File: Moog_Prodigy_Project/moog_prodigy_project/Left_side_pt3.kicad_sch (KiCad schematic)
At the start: 58 parts, among them SW7 SW_Slide_DPDT, U12B MCP6562, U13 NE5532, U14 AD8001AR, U14C BF244A, U14E? 4007, U2 NE5532, U2B2 OPA134

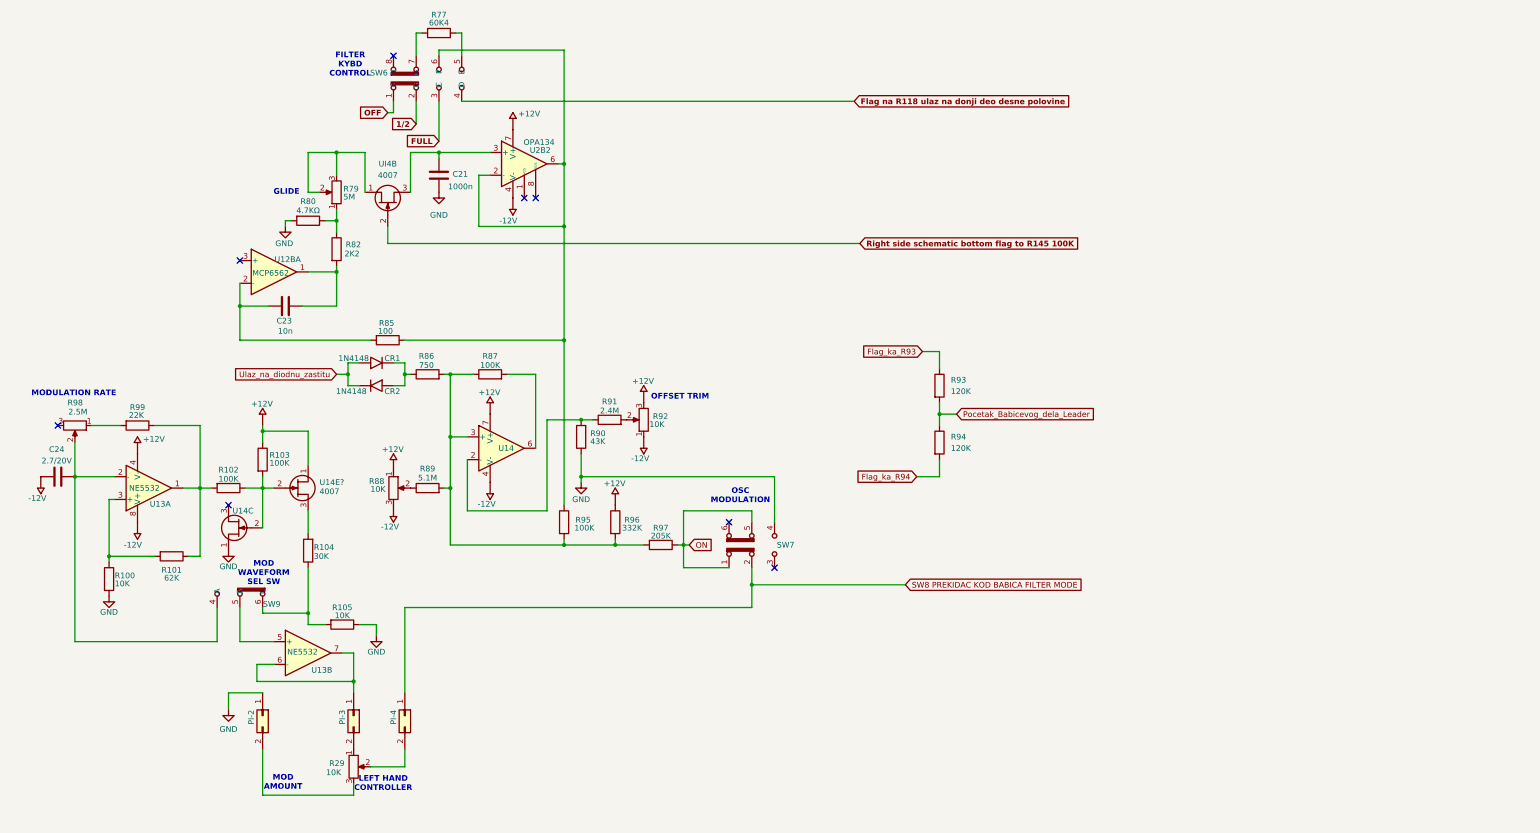
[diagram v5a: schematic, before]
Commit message: KiCad smybols import CA3046
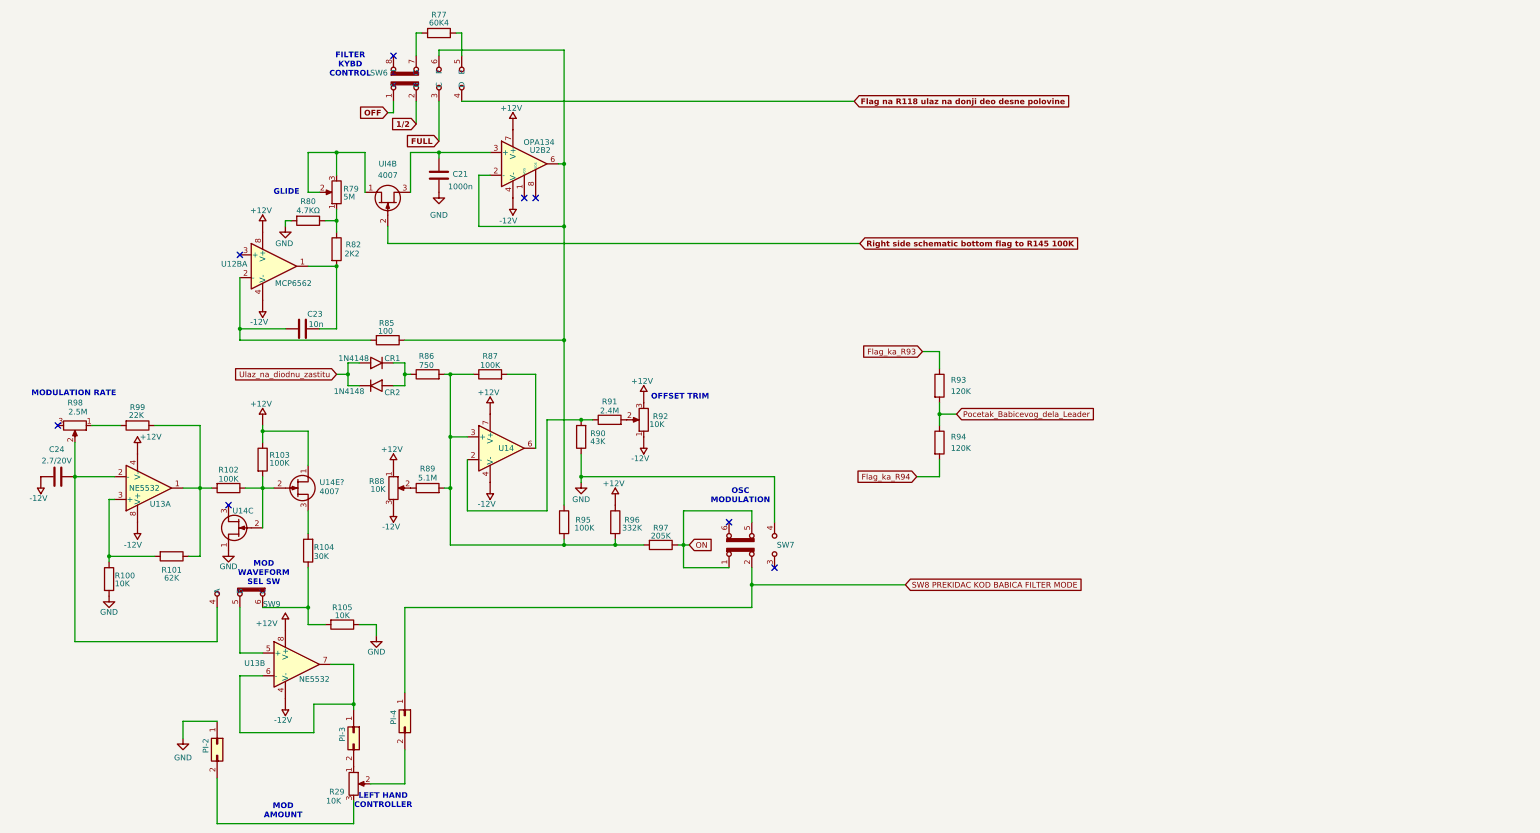
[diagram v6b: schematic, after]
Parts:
- removed Vcc__minus_17, Vcc__minus_20: -12V, symbol power:napajanje
- removed Vcc__plus_13, Vcc__plus_17, Vcc__plus_24, Vcc__plus_25, Vcc__plus_26, Vcc__plus_27, Vcc__plus_28: +12V, symbol power:napajanje
- added unit 3 of U13
- added U34, U35, U36, U37, U38, U39, U40, U68, U72: +12V, symbol Power_supply:Vcc_reference
- added U67: MCP6562, symbol Comparator:MCP6562
- added U69, U70, U71: -12V, symbol Power_supply:Vcc_reference
- added Vcc__minus_1: -12V, symbol power:napajanje
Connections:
- net at R103.1, U14E?.1 (D): now also U38.
- net at U2B2.7 (V+): now also U34.
- net at R96.1: now also U36.
- net at U14.7 (V+): now also U40.
- net at R88.1: now also U37.
- net at C24.2: now also U70.
- net at R88.3: now also U71.
- net at U2.4 (V-): now also U39.
- net at R92.3: now also U35.
- new net: U67.4 (V-), Vcc__minus_1.
- new net: U67.8 (V+), U68.
- new net: U13.8 (V+), U72.
- new net: U13.4 (V-), U69.
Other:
- moved on the sheet: C23, PI-2, PI-3, R29, U12BA, U13B

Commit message: Vcc fix, banana jack, connector, OP adding top sch
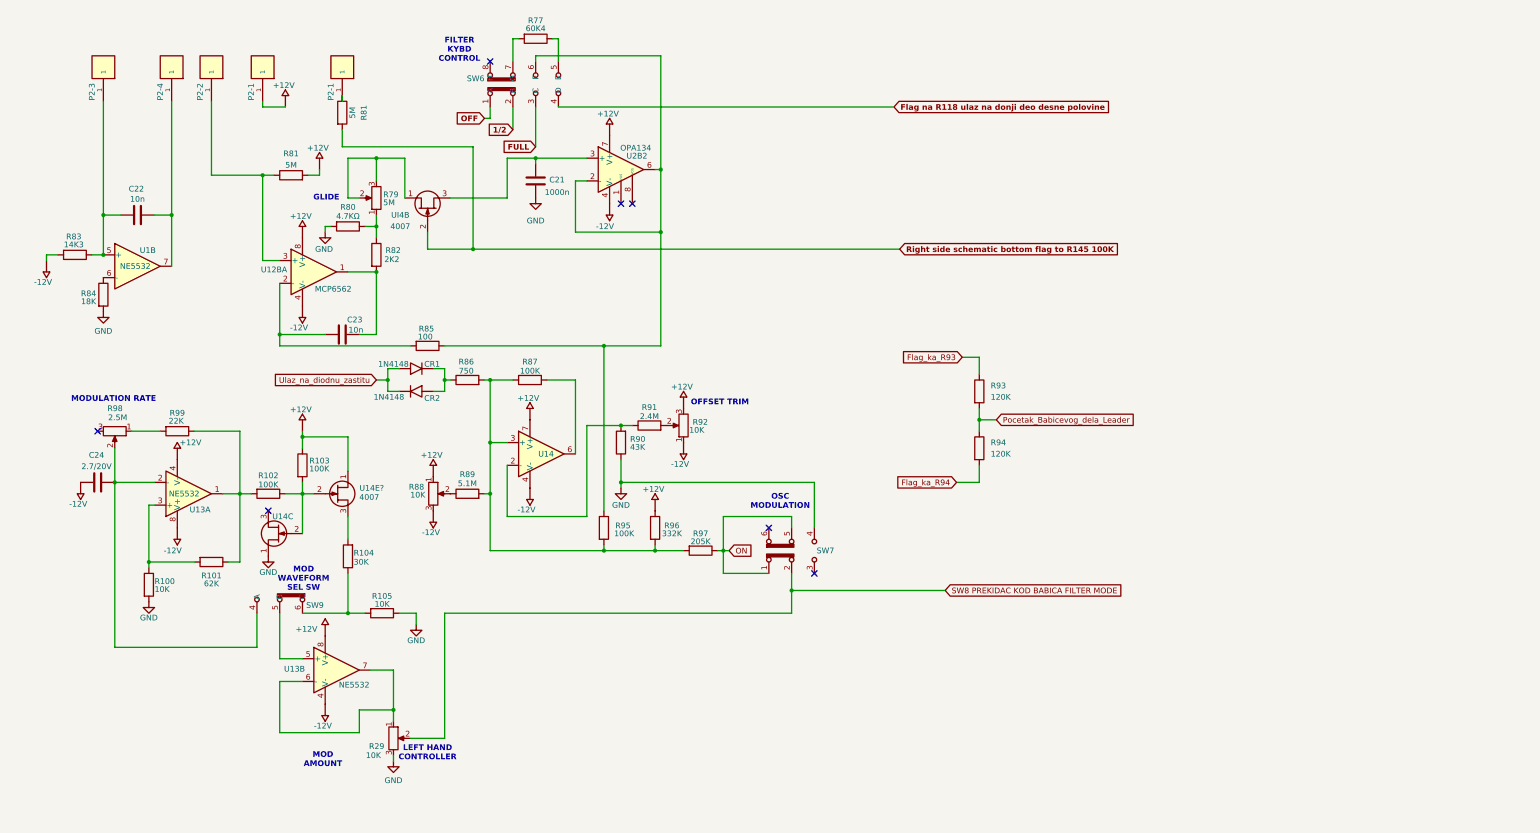
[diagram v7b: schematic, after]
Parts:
- removed PI-2, PI-3, PI-4: Conn_02x01, symbol Connector_Generic:Conn_02x01
- added C22: 10n, symbol Device:C
- added J1: P2-3, CT3151-2:CALTEST_CT3151-2, symbol CT3151-2:CT3151-2
- added J2: P2-4, CT3151-2:CALTEST_CT3151-2, symbol CT3151-2:CT3151-2
- added J3: P2-2, CT3151-2:CALTEST_CT3151-2, symbol CT3151-2:CT3151-2
- added J4, J5: P2-1, CT3151-2:CALTEST_CT3151-2, symbol CT3151-2:CT3151-2
- added R81 (x2): 5M, symbol Device:R
- added R83: 14K3, symbol Device:R
- added R84: 18K, symbol Device:R
- added U1: NE5532, symbol Amplifier_Operational:NE5532
- added U73, U74: +12V, symbol Power_supply:Vcc_reference
- added Vcc__minus_2: -12V, symbol power:napajanje
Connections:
- net GND: now also R29.3, R84.2
- net Right side schematic bottom flag to R145 100K: now also R81.2
- net SW8 PREKIDAC KOD BABICA FILTER MODE: now also R29.2
- net at U13.6 (-), U13.7: now also R29.1
- net at U12B.3 (+): now also J3.1, J3.2 (1), J3.3 (1), J3.4 (1), R81.1
- new net: J5.1, J5.2 (1), J5.3 (1), J5.4 (1), U74.
- new net: R84.1, U1.6 (-)
- new net: C22.2, J1.1, J1.2 (1), J1.3 (1), J1.4 (1), R83.1, U1.5 (+)
- new net: R83.2, Vcc__minus_2.
- new net: J4.1, J4.2 (1), J4.3 (1), J4.4 (1), R81.1
- new net: R81.2, U73.
- new net: C22.1, J2.1, J2.2 (1), J2.3 (1), J2.4 (1), U1.7
- no-connect marks 8 -> 7
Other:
- moved on the sheet: C21, C23, C24, CR1, CR2, R100, R101, R102, R103, R104, R105, R29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

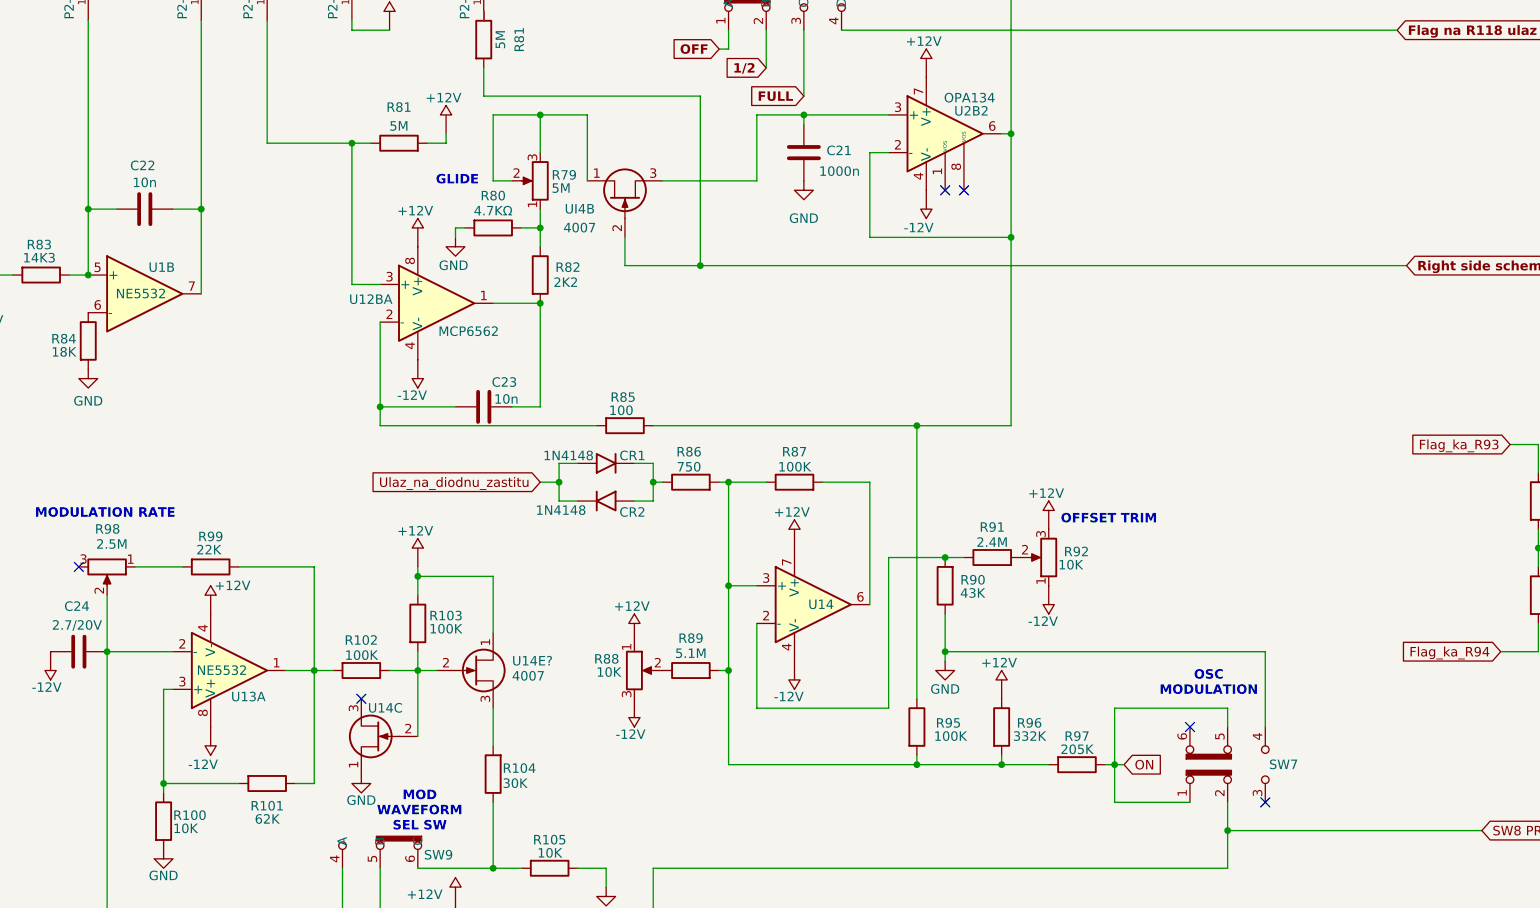
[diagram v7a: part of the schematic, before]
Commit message: 4007 update, impor biblioteka LM 393
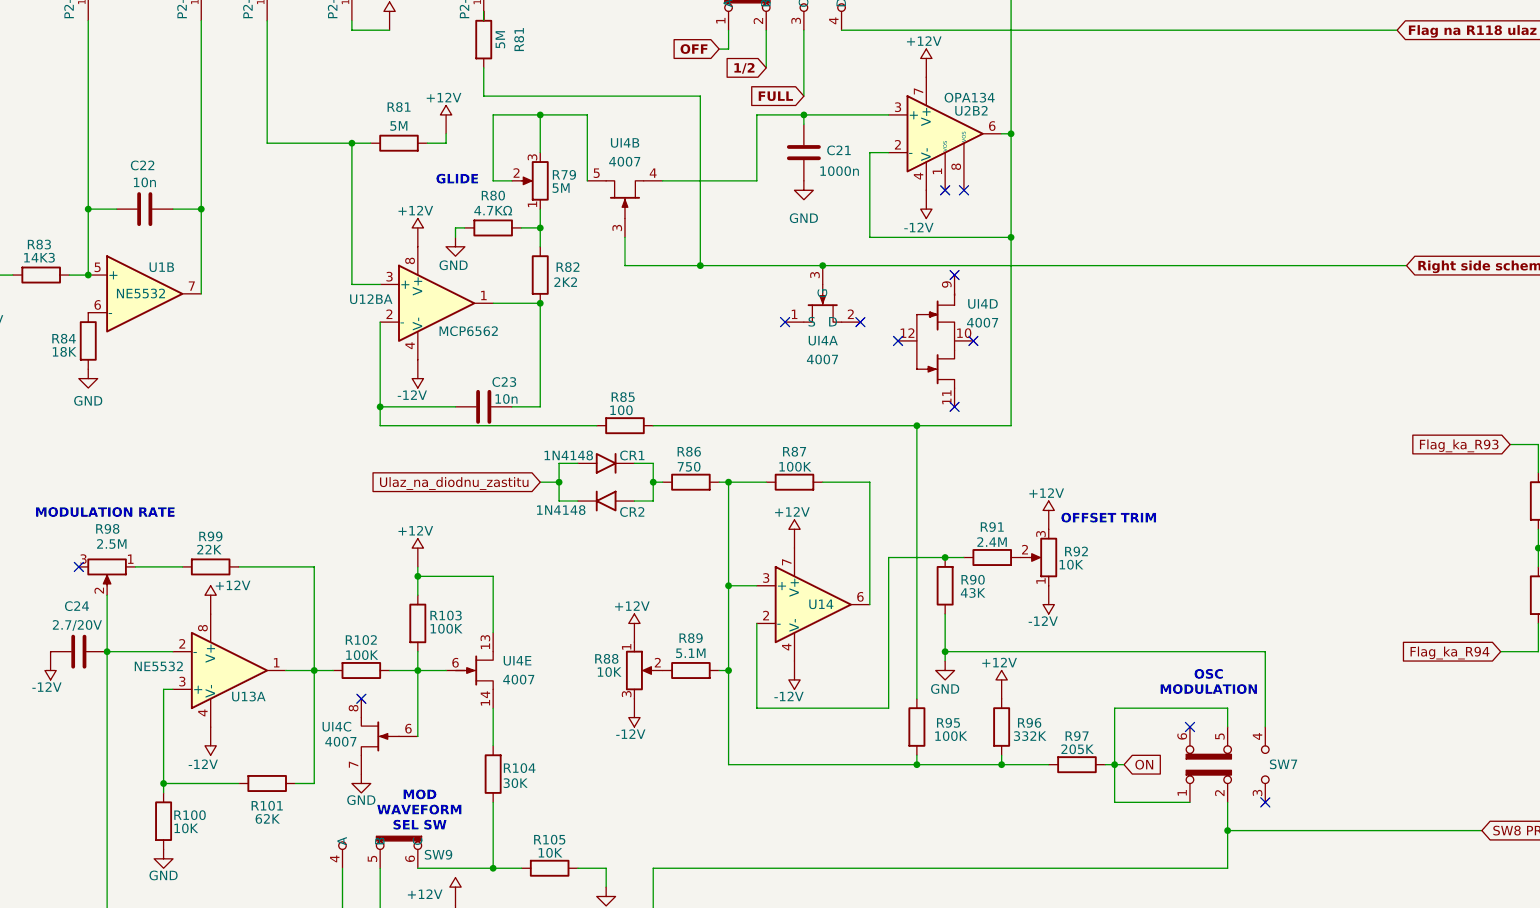
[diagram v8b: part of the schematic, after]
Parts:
- removed U14C: BF244A, Package_TO_SOT_THT:TO-92_Inline, symbol Transistor_FET:BF244A
- removed U14E?, UI4B: 4007, Package_TO_SOT_THT:TO-92_Inline, symbol Transistor_FET:BF244A
- added UI4: 4007, symbol Transistor_FET:4007_Novi
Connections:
- net GND: now also UI4.7
- net Right side schematic bottom flag to R145 100K: now also UI4.3, UI4.3 (G)
- net at R79.2, R79.3: now also UI4.5
- net at C21.2, U2B2.3 (+): now also UI4.4
- net at R103.1, U38.: now also UI4.13
- net at R102.1, R103.2: now also UI4.6, UI4.6
- net at R104.2: now also UI4.14
- net at U39.: now also U2.8 (V+); no longer U2.4 (V-)
- net at Vcc__minus_15.: now also U2.4 (V-); no longer U2.8 (V+)
- no-connect marks 7 -> 13
